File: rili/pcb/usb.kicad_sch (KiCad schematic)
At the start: 8 parts, among them J3 USB_C_Receptacle_USB2.0_16P, U2 USBLC6-2SC6, U7 CH334R

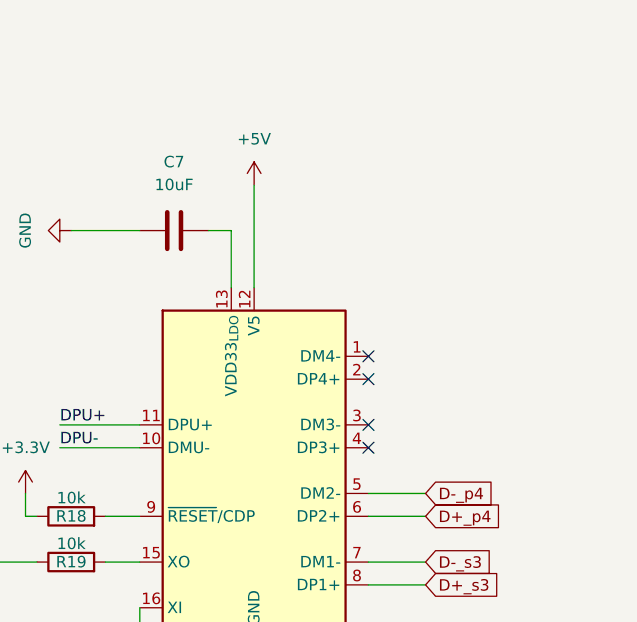
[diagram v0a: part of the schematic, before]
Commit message: schéma v2 : coffre P4 complet — ERC 0 erreur
- Feuille p4 (ex sans_titre) : AMS1117-3.3 (rail P4_3V3 séparé, 10µF/22µF),
  CHIP_PU RC 100k+100nF, USB HS (ESP_USB_P/N) vers le port 2 du hub,
  microSD slot UHS-I (CLK/CMD/DAT0-3 sur GPIO39-44, pull-ups 10k),
  prog P4 via port 3 du hub (USB-Serial-JTAG + jumpers d'isolation)
- Périphériques : écran Sharp LS011B7DH03 (SPI partagé, CS_DPL=GPIO14),
  trackpad TPS43 (I2C 47/48, RDY=42, bloc généré+validé), C6 laissé vierge
  (OTA via P4 = voie officielle)
- Ménage ERC : 65 no_connect + 6 PWR_FLAG posés par script (fix_nc.py),
  labels fantômes S3P4 supprimés — ERC projet : 71 → 0 erreur,
  warnings 262 → 158 (ratchet enregistré)
- Hooks Claude Code Stop/PostToolUse désactivés (garde-fou = pre-push + CI)

Reste au schéma : le 2e MCU (moitié droite, col*_d/row*_d en attente).
DRC layout hors périmètre (chantier séparé).

Co-Authored-By: Claude Fable 5 <noreply@anthropic.com>
Claude-Session: https://claude.ai/code/session_01GfX5RmekmQi78Dm37qsT4Z
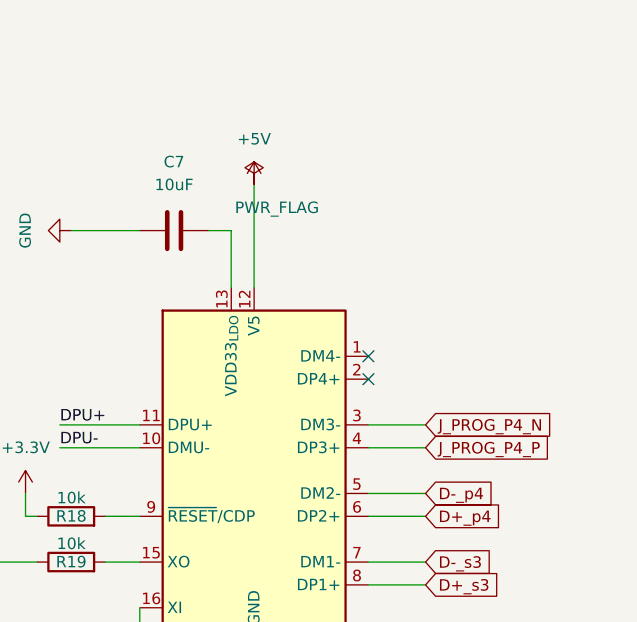
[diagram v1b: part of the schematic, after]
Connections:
- net J_PROG_P4_N: now reaches U7.3 (DM3-)
- net J_PROG_P4_P: now reaches U7.4 (DP3+)
- no-connect marks 6 -> 4
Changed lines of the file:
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@@
-	)
-	(no_connect
-		(at 82.55 138.43)
-	)
-	(no_connect
-		(at 82.55 140.97)
 	)
 	(no_connect
@@
 	(wire
 		(pts
+			(xy 88.9 138.43) (xy 82.55 138.43)
+		)
+		(stroke
+			(width 0)
+			(type default)
+		)
+	)
+	(wire
+		(pts
 			(xy 88.9 156.21) (xy 82.55 156.21)
 		)
@@
 		(pts
 			(xy 67.31 116.84) (xy 67.31 123.19)
+		)
+		(stroke
+			(width 0)
+			(type default)
+		)
+	)
+	(wire
+		(pts
+			(xy 88.9 140.97) (xy 82.55 140.97)
 		)
 		(stroke
@@
 			)
 			(justify left bottom)
+		)
+	)
+	(global_label "J_PROG_P4_N"
+		(shape input)
+		(at 88.9 138.43 0)
+		(fields_autoplaced yes)
+		(effects
+			(font
+				(size 1.27 1.27)
+			)
+			(justify left)
+		)
+		(property "Intersheetrefs" "${INTERSHEET_REFS}"
+			(at 104.0519 138.43 0)
+			(hide yes)
+			(show_name no)
+			(do_not_autoplace no)
+			(effects
+				(font
+					(size 1.27 1.27)
+				)
+				(justify left)
+			)
 		)
 	)
@@
 		(property "Intersheetrefs" "${INTERSHEET_REFS}"
 			(at 97.3995 146.05 0)
+			(hide yes)
+			(show_name no)
+			(do_not_autoplace no)
+			(effects
+				(font
+					(size 1.27 1.27)
+				)
+				(justify left)
+			)
+		)
+	)
+	(global_label "J_PROG_P4_P"
+		(shape input)
+		(at 88.9 140.97 0)
+		(fields_autoplaced yes)
+		(effects
+			(font
+				(size 1.27 1.27)
+			)
+			(justify left)
+		)
+		(property "Intersheetrefs" "${INTERSHEET_REFS}"
+			(at 103.9914 140.97 0)
 			(hide yes)
 			(show_name no)
@@
 		)
 		(instances
-			(project "rili"
+			(project "niphar"
 				(path "/7138aad8-3c5f-41d0-9987-adc2f08f0576/c05a1138-8c6c-44e2-ac38-1bed4028aa56"
 					(reference "R16")
+					(unit 1)
+				)
+			)
+		)
+	)
+	(symbol
+		(lib_id "power:PWR_FLAG")
+		(at 69.85 111.76 0)
+		(unit 1)
+		(body_style 1)
+		(exclude_from_sim no)
+		(in_bom yes)
+		(on_board yes)
+		(in_pos_files yes)
+		(dnp no)
+		(property "Reference" "#FLG0973"
+			(at 72.39 111.76 0)
+			(hide yes)
+			(show_name no)
+			(do_not_autoplace no)
+			(effects
+				(font
+					(size 1.27 1.27)
+				)
+			)
+		)
+		(property "Value" "PWR_FLAG"
+			(at 72.39 114.3 0)
+			(show_name no)
+			(do_not_autoplace no)
+			(effects
+				(font
+					(size 1.27 1.27)
+				)
+			)
+		)
+		(property "Footprint" ""
+			(at 69.85 111.76 0)
+			(hide yes)
+			(show_name no)
+			(do_not_autoplace no)
+			(effects
+				(font
+					(size 1.27 1.27)
+				)
+			)
+		)
+		(property "Datasheet" ""
+			(at 69.85 111.76 0)
+			(hide yes)
+			(show_name no)
+			(do_not_autoplace no)
+			(effects
+				(font
+					(size 1.27 1.27)
+				)
+			)
+		)
+		(property "Description" ""
+			(at 69.85 111.76 0)
+			(show_name no)
+			(do_not_autoplace no)
+			(effects
+				(font
+					(size 1.27 1.27)
+				)
+			)
+		)
+		(pin "1"
+		)
+		(instances
+			(project "niphar"
+				(path "/7138aad8-3c5f-41d0-9987-adc2f08f0576/c05a1138-8c6c-44e2-ac38-1bed4028aa56"
+					(reference "#FLG0973")
 					(unit 1)
 				)
@@
 		)
 		(instances
-			(project "rili"
+			(project "niphar"
 				(path "/7138aad8-3c5f-41d0-9987-adc2f08f0576/c05a1138-8c6c-44e2-ac38-1bed4028aa56"
 					(reference "#PWR053")
@@
 		)
 		(instances
-			(project "rili"
+			(project "niphar"
 				(path "/7138aad8-3c5f-41d0-9987-adc2f08f0576/c05a1138-8c6c-44e2-ac38-1bed4028aa56"
 					(reference "U2")
@@
 		)
 		(instances
-			(project "rili"
+			(project "niphar"
 				(path "/7138aad8-3c5f-41d0-9987-adc2f08f0576/c05a1138-8c6c-44e2-ac38-1bed4028aa56"
 					(reference "#PWR056")
@@
 		)
 		(instances
-			(project "rili"
+			(project "niphar"
 				(path "/7138aad8-3c5f-41d0-9987-adc2f08f0576/c05a1138-8c6c-44e2-ac38-1bed4028aa56"
 					(reference "#PWR013")
@@
 		)
 		(instances
-			(project "rili"
+			(project "niphar"
 				(path "/7138aad8-3c5f-41d0-9987-adc2f08f0576/c05a1138-8c6c-44e2-ac38-1bed4028aa56"
 					(reference "#PWR057")
@@
 		)
 		(instances
-			(project "rili"
+			(project "niphar"
 				(path "/7138aad8-3c5f-41d0-9987-adc2f08f0576/c05a1138-8c6c-44e2-ac38-1bed4028aa56"
 					(reference "R17")
@@
 		)
 		(instances
-			(project "rili"
+			(project "niphar"
 				(path "/7138aad8-3c5f-41d0-9987-adc2f08f0576/c05a1138-8c6c-44e2-ac38-1bed4028aa56"
 					(reference "#PWR055")
@@
 		)
 		(instances
-			(project "rili"
+			(project "niphar"
 				(path "/7138aad8-3c5f-41d0-9987-adc2f08f0576/c05a1138-8c6c-44e2-ac38-1bed4028aa56"
 					(reference "#PWR04")
@@
 		)
 		(instances
-			(project "rili"
+			(project "niphar"
 				(path "/7138aad8-3c5f-41d0-9987-adc2f08f0576/c05a1138-8c6c-44e2-ac38-1bed4028aa56"
 					(reference "#PWR054")
@@
 		)
 		(instances
-			(project "rili"
+			(project "niphar"
 				(path "/7138aad8-3c5f-41d0-9987-adc2f08f0576/c05a1138-8c6c-44e2-ac38-1bed4028aa56"
 					(reference "J3")
@@
 		)
 		(instances
-			(project "rili"
+			(project "niphar"
 				(path "/7138aad8-3c5f-41d0-9987-adc2f08f0576/c05a1138-8c6c-44e2-ac38-1bed4028aa56"
 					(reference "C7")
@@
 		)
 		(instances
-			(project "rili"
+			(project "niphar"
 				(path "/7138aad8-3c5f-41d0-9987-adc2f08f0576/c05a1138-8c6c-44e2-ac38-1bed4028aa56"
 					(reference "#PWR058")
@@
 		)
 		(instances
-			(project "rili"
+			(project "niphar"
 				(path "/7138aad8-3c5f-41d0-9987-adc2f08f0576/c05a1138-8c6c-44e2-ac38-1bed4028aa56"
 					(reference "R18")
@@
 		)
 		(instances
-			(project "rili"
+			(project "niphar"
 				(path "/7138aad8-3c5f-41d0-9987-adc2f08f0576/c05a1138-8c6c-44e2-ac38-1bed4028aa56"
 					(reference "U7")
@@
 		)
 		(instances
-			(project "rili"
+			(project "niphar"
 				(path "/7138aad8-3c5f-41d0-9987-adc2f08f0576/c05a1138-8c6c-44e2-ac38-1bed4028aa56"
 					(reference "R19")
@@
 		)
 		(instances
-			(project "rili"
+			(project "niphar"
 				(path "/7138aad8-3c5f-41d0-9987-adc2f08f0576/c05a1138-8c6c-44e2-ac38-1bed4028aa56"
 					(reference "#PWR051")

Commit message: layout v2 : carte routée — PCB↔schéma réconciliés, BOM LCSC, TVS matrice, DRC 990→24
- réconciliation PCB↔schéma en une passe : 105 empreintes remariées (matrice ×2,
  module P4), 54 périmées supprimées, ~140 importées par F8 ; footprint TRRS
  MJ-4PP-9_rev3 créé (pads mappés de l'ancien design fonctionnel)
- placement : moitié droite générée au miroir exact du pré-placement gauche
  (axe x=188.46048), trous de montage symétrisés, origine de grille sur l'axe
- protection ESD matrice : 22 SD05C-01F (un par ligne, côté switchs des 100R,
  validés par partition de netlist) ; PWR_FLAG +5V_D réparé
- BOM LCSC dans les propriétés des symboles (32 composants : réfs, liens,
  notes d'achat) + annexe courses complète au plan v2 ; connecteur trackpad
  corrigé (ZIF Hirose FH12-6S-0.5SH, réf MNT Reform)
- règles JLCPCB (planchers DRC + classes Default/Power re-branchées v2),
  passage 4 couches, routage complet des deux moitiés
- gerbers v1 corne-cherry retirés (obsolètes)
- baselines tripwire re-référencées : DRC 990→24 erreurs / 208→17 warnings,
  ERC 0 erreur / 200 warnings (53 fantômes headless documentés)

Co-Authored-By: Claude Fable 5 <noreply@anthropic.com>
Claude-Session: https://claude.ai/code/session_01GfX5RmekmQi78Dm37qsT4Z
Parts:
- J8: renamed from J3; footprint (none) -> Connector_USB:USB_C_Receptacle_HRO_TYPE-C-31-M-12; LCSC (none) -> C165948; Lien (none) -> https://lcsc.com/product-detail/C165948.html
- R48: renamed from R18; footprint Resistor_SMD:R_0201_0603Metric_Pad0.64x0.40mm_HandSolder -> Resistor_SMD:R_0603_1608Metric_Pad0.98x0.95mm_HandSolder
- R49: renamed from R19; footprint Resistor_SMD:R_0201_0603Metric_Pad0.64x0.40mm_HandSolder -> Resistor_SMD:R_0603_1608Metric_Pad0.98x0.95mm_HandSolder
- U13: renamed from U7; LCSC (none) -> C4154405; Lien (none) -> https://lcsc.com/product-detail/C4154405.html
- U14: renamed from U2; LCSC (none) -> C7519; Lien (none) -> https://lcsc.com/product-detail/C7519.html
- renumbered C7 to C13, R16 to R50, R17 to R52
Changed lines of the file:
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@@
 		(dnp no)
 		(fields_autoplaced yes)
-		(property "Reference" "R16"
+		(property "Reference" "R50"
 			(at 63.5 29.21 90)
 			(show_name no)
@@
 			(project "niphar"
 				(path "/7138aad8-3c5f-41d0-9987-adc2f08f0576/c05a1138-8c6c-44e2-ac38-1bed4028aa56"
-					(reference "R16")
+					(reference "R50")
 					(unit 1)
 				)
@@
 		(in_pos_files yes)
 		(dnp no)
-		(property "Reference" "#FLG0973"
+		(property "Reference" "#FLG02"
 			(at 72.39 111.76 0)
 			(hide yes)
@@
 			(project "niphar"
 				(path "/7138aad8-3c5f-41d0-9987-adc2f08f0576/c05a1138-8c6c-44e2-ac38-1bed4028aa56"
-					(reference "#FLG0973")
+					(reference "#FLG02")
 					(unit 1)
 				)
@@
 		(dnp no)
 		(fields_autoplaced yes)
-		(property "Reference" "#PWR053"
+		(property "Reference" "#PWR058"
 			(at 74.93 43.18 0)
 			(hide yes)
@@
 			(project "niphar"
 				(path "/7138aad8-3c5f-41d0-9987-adc2f08f0576/c05a1138-8c6c-44e2-ac38-1bed4028aa56"
-					(reference "#PWR053")
+					(reference "#PWR058")
 					(unit 1)
 				)
@@
 		(in_pos_files yes)
 		(dnp no)
-		(property "Reference" "U2"
+		(property "Reference" "U14"
 			(at 86.7411 38.1 0)
 			(show_name no)
@@
 			)
 		)
+		(property "LCSC" "C7519"
+			(at 85.09 45.72 0)
+			(hide yes)
+			(show_name no)
+			(do_not_autoplace no)
+			(effects
+				(font
+					(size 1.27 1.27)
+				)
+			)
+		)
+		(property "Lien" "https://lcsc.com/product-detail/C7519.html"
+			(at 85.09 45.72 0)
+			(hide yes)
+			(show_name no)
+			(do_not_autoplace no)
+			(effects
+				(font
+					(size 1.27 1.27)
+				)
+			)
+		)
 		(pin "3"
 		)
@@
 			(project "niphar"
 				(path "/7138aad8-3c5f-41d0-9987-adc2f08f0576/c05a1138-8c6c-44e2-ac38-1bed4028aa56"
-					(reference "U2")
+					(reference "U14")
 					(unit 1)
 				)
@@
 		(dnp no)
 		(fields_autoplaced yes)
-		(property "Reference" "#PWR056"
+		(property "Reference" "#PWR063"
 			(at 85.09 66.04 0)
 			(hide yes)
@@
 			(project "niphar"
 				(path "/7138aad8-3c5f-41d0-9987-adc2f08f0576/c05a1138-8c6c-44e2-ac38-1bed4028aa56"
-					(reference "#PWR056")
+					(reference "#PWR063")
 					(unit 1)
 				)
@@
 		(dnp no)
 		(fields_autoplaced yes)
-		(property "Reference" "#PWR013"
+		(property "Reference" "#PWR057"
 			(at 69.85 175.26 0)
 			(hide yes)
@@
 			(project "niphar"
 				(path "/7138aad8-3c5f-41d0-9987-adc2f08f0576/c05a1138-8c6c-44e2-ac38-1bed4028aa56"
-					(reference "#PWR013")
+					(reference "#PWR057")
 					(unit 1)
 				)
@@
 		(dnp no)
 		(fields_autoplaced yes)
-		(property "Reference" "#PWR057"
+		(property "Reference" "#PWR054"
 			(at 44.45 149.86 0)
 			(hide yes)
@@
 			(project "niphar"
 				(path "/7138aad8-3c5f-41d0-9987-adc2f08f0576/c05a1138-8c6c-44e2-ac38-1bed4028aa56"
-					(reference "#PWR057")
+					(reference "#PWR054")
 					(unit 1)
 				)
@@
 		(in_pos_files yes)
 		(dnp no)
-		(property "Reference" "R17"
+		(property "Reference" "R52"
 			(at 63.5 44.45 90)
 			(show_name no)
@@
 			(project "niphar"
 				(path "/7138aad8-3c5f-41d0-9987-adc2f08f0576/c05a1138-8c6c-44e2-ac38-1bed4028aa56"
-					(reference "R17")
+					(reference "R52")
 					(unit 1)
 				)
@@
 		(dnp no)
 		(fields_autoplaced yes)
-		(property "Reference" "#PWR055"
+		(property "Reference" "#PWR061"
 			(at 85.09 30.48 0)
 			(hide yes)
@@
 			(project "niphar"
 				(path "/7138aad8-3c5f-41d0-9987-adc2f08f0576/c05a1138-8c6c-44e2-ac38-1bed4028aa56"
-					(reference "#PWR055")
+					(reference "#PWR061")
 					(unit 1)
 				)
@@
 		(dnp no)
 		(fields_autoplaced yes)
-		(property "Reference" "#PWR04"
+		(property "Reference" "#PWR056"
 			(at 69.85 115.57 0)
 			(hide yes)
@@
 			(project "niphar"
 				(path "/7138aad8-3c5f-41d0-9987-adc2f08f0576/c05a1138-8c6c-44e2-ac38-1bed4028aa56"
-					(reference "#PWR04")
+					(reference "#PWR056")
 					(unit 1)
 				)
@@
 		(dnp no)
 		(fields_autoplaced yes)
-		(property "Reference" "#PWR054"
+		(property "Reference" "#PWR052"
 			(at 33.02 74.93 0)
 			(hide yes)
@@
 			(project "niphar"
 				(path "/7138aad8-3c5f-41d0-9987-adc2f08f0576/c05a1138-8c6c-44e2-ac38-1bed4028aa56"
-					(reference "#PWR054")
+					(reference "#PWR052")
 					(unit 1)
 				)
@@
 		(dnp no)
 		(fields_autoplaced yes)
-		(property "Reference" "J3"
+		(property "Reference" "J8"
 			(at 33.02 22.86 0)
 			(show_name no)
@@
 			)
 		)
-		(property "Footprint" ""
+		(property "Footprint" "Connector_USB:USB_C_Receptacle_HRO_TYPE-C-31-M-12"
 			(at 36.83 45.72 0)
 			(hide yes)
@@
 			)
 		)
+		(property "LCSC" "C165948"
+			(at 33.02 45.72 0)
+			(hide yes)
+			(show_name no)
+			(do_not_autoplace no)
+			(effects
+				(font
+					(size 1.27 1.27)
+				)
+			)
+		)
+		(property "Lien" "https://lcsc.com/product-detail/C165948.html"
+			(at 33.02 45.72 0)
+			(hide yes)
+			(show_name no)
+			(do_not_autoplace no)
+			(effects
+				(font
+					(size 1.27 1.27)
+				)
+			)
+		)
 		(pin "B7"
 		)
@@
 			(project "niphar"
 				(path "/7138aad8-3c5f-41d0-9987-adc2f08f0576/c05a1138-8c6c-44e2-ac38-1bed4028aa56"
-					(reference "J3")
+					(reference "J8")
 					(unit 1)
 				)
@@
 		(dnp no)
 		(fields_autoplaced yes)
-		(property "Reference" "C7"
+		(property "Reference" "C13"
 			(at 60.96 109.22 90)
 			(show_name no)
@@
 			(project "niphar"
 				(path "/7138aad8-3c5f-41d0-9987-adc2f08f0576/c05a1138-8c6c-44e2-ac38-1bed4028aa56"
-					(reference "C7")
+					(reference "C13")
 					(unit 1)
 				)
@@
 		(dnp no)
 		(fields_autoplaced yes)
-		(property "Reference" "#PWR058"
+		(property "Reference" "#PWR053"
 			(at 38.1 149.86 0)
 			(hide yes)
@@
 			(project "niphar"
 				(path "/7138aad8-3c5f-41d0-9987-adc2f08f0576/c05a1138-8c6c-44e2-ac38-1bed4028aa56"
-					(reference "#PWR058")
+					(reference "#PWR053")
 					(unit 1)
 				)
@@
 		(in_pos_files yes)
 		(dnp no)
-		(property "Reference" "R18"
+		(property "Reference" "R48"
 			(at 49.53 148.59 90)
 			(show_name no)
@@
 			)
 		)
-		(property "Footprint" "Resistor_SMD:R_0201_0603Metric_Pad0.64x0.40mm_HandSolder"
+		(property "Footprint" "Resistor_SMD:R_0603_1608Metric_Pad0.98x0.95mm_HandSolder"
 			(at 49.53 150.368 90)
 			(hide yes)
@@
 			(project "niphar"
 				(path "/7138aad8-3c5f-41d0-9987-adc2f08f0576/c05a1138-8c6c-44e2-ac38-1bed4028aa56"
-					(reference "R18")
+					(reference "R48")
 					(unit 1)
 				)
@@
 		(dnp no)
 		(fields_autoplaced yes)
-		(property "Reference" "U7"
+		(property "Reference" "U13"
 			(at 71.9933 163.83 0)
 			(show_name no)
@@
 			)
 		)
+		(property "LCSC" "C4154405"
+			(at 69.85 143.51 0)
+			(hide yes)
+			(show_name no)
+			(do_not_autoplace no)
+			(effects
+				(font
+					(size 1.27 1.27)
+				)
+			)
+		)
+		(property "Lien" "https://lcsc.com/product-detail/C4154405.html"
+			(at 69.85 143.51 0)
+			(hide yes)
+			(show_name no)
+			(do_not_autoplace no)
+			(effects
+				(font
+					(size 1.27 1.27)
+				)
+			)
+		)
 		(pin "3"
 		)
@@
 			(project "niphar"
 				(path "/7138aad8-3c5f-41d0-9987-adc2f08f0576/c05a1138-8c6c-44e2-ac38-1bed4028aa56"
-					(reference "U7")
+					(reference "U13")
 					(unit 1)
 				)
@@
 		(in_pos_files yes)
 		(dnp no)
-		(property "Reference" "R19"
+		(property "Reference" "R49"
 			(at 49.53 153.67 90)
 			(show_name no)
@@
 			)
 		)
-		(property "Footprint" "Resistor_SMD:R_0201_0603Metric_Pad0.64x0.40mm_HandSolder"
+		(property "Footprint" "Resistor_SMD:R_0603_1608Metric_Pad0.98x0.95mm_HandSolder"
 			(at 49.53 155.448 90)
 			(hide yes)
@@
 			(project "niphar"
 				(path "/7138aad8-3c5f-41d0-9987-adc2f08f0576/c05a1138-8c6c-44e2-ac38-1bed4028aa56"
-					(reference "R19")
+					(reference "R49")
 					(unit 1)
 				)
@@
 		(dnp no)
 		(fields_autoplaced yes)
-		(property "Reference" "#PWR051"
+		(property "Reference" "#PWR055"
 			(at 43.18 116.84 0)
 			(hide yes)
@@
 			(project "niphar"
 				(path "/7138aad8-3c5f-41d0-9987-adc2f08f0576/c05a1138-8c6c-44e2-ac38-1bed4028aa56"
-					(reference "#PWR051")
-					(unit 1)
-				)
+					(reference "#PWR055")
+					(unit 1)
+				)

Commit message: review : solde complet — Tip TRRS protégé, condos +BATT, prog P4 dégagée
- TVS Tip : canal 3 des SRV05 relié au Tip des deux jacks (net TIP_5V, validé
  netlist : jack.T + load switch OUT + SRV05 sans toucher LINK_5V_EN)
- C29/C30 : 10µF sur +BATT/+BATT_D près des TP4056, placés et routés par Mae
- R48/R49 supprimés par Mae (CH334R : pull-up RESET# interne 25k, mode
  sans-quartz XO flottant conforme datasheet, fuite batterie→hub éliminée)
- pistes JP1/JP2 (prog USB du P4) écartées de la zone GND : zéro violation
- nettoyage : no_connect orpheline de la dépose R48/R49
- DRC 36/26 → 17/22 (ménage de routage par Mae), ratchet enregistré

Décisions documentées : SD manipulée hors tension (pas de TVS SD), tables de
pins matrice réelles + conventions firmware en annexe du plan v2.

Co-Authored-By: Claude Fable 5 <noreply@anthropic.com>
Claude-Session: https://claude.ai/code/session_01GfX5RmekmQi78Dm37qsT4Z
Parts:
- removed R48, R49: 10k, Resistor_SMD:R_0603_1608Metric_Pad0.98x0.95mm_HandSolder, symbol Device:R
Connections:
- no-connect marks 4 -> 6
